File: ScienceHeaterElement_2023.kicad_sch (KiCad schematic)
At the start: 1 part, among them U1 LMT85DCK

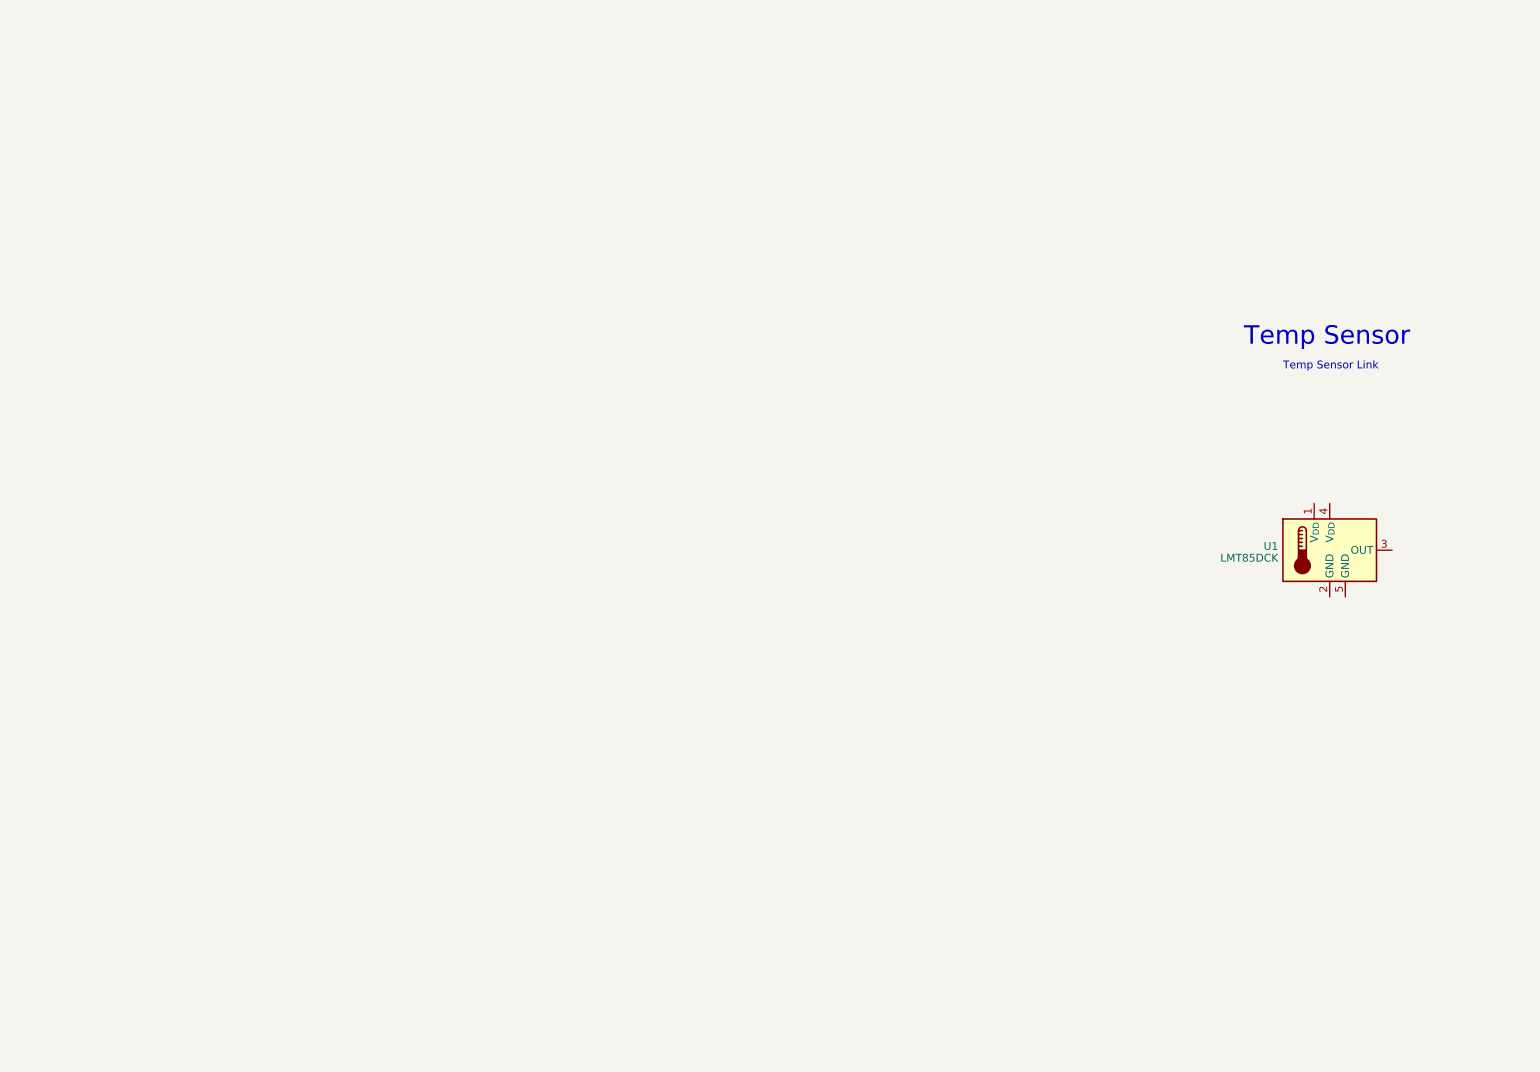
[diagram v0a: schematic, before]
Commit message: Science Heater KiCad
Inserted Anderson components, a temperature sensor and a molex SL.
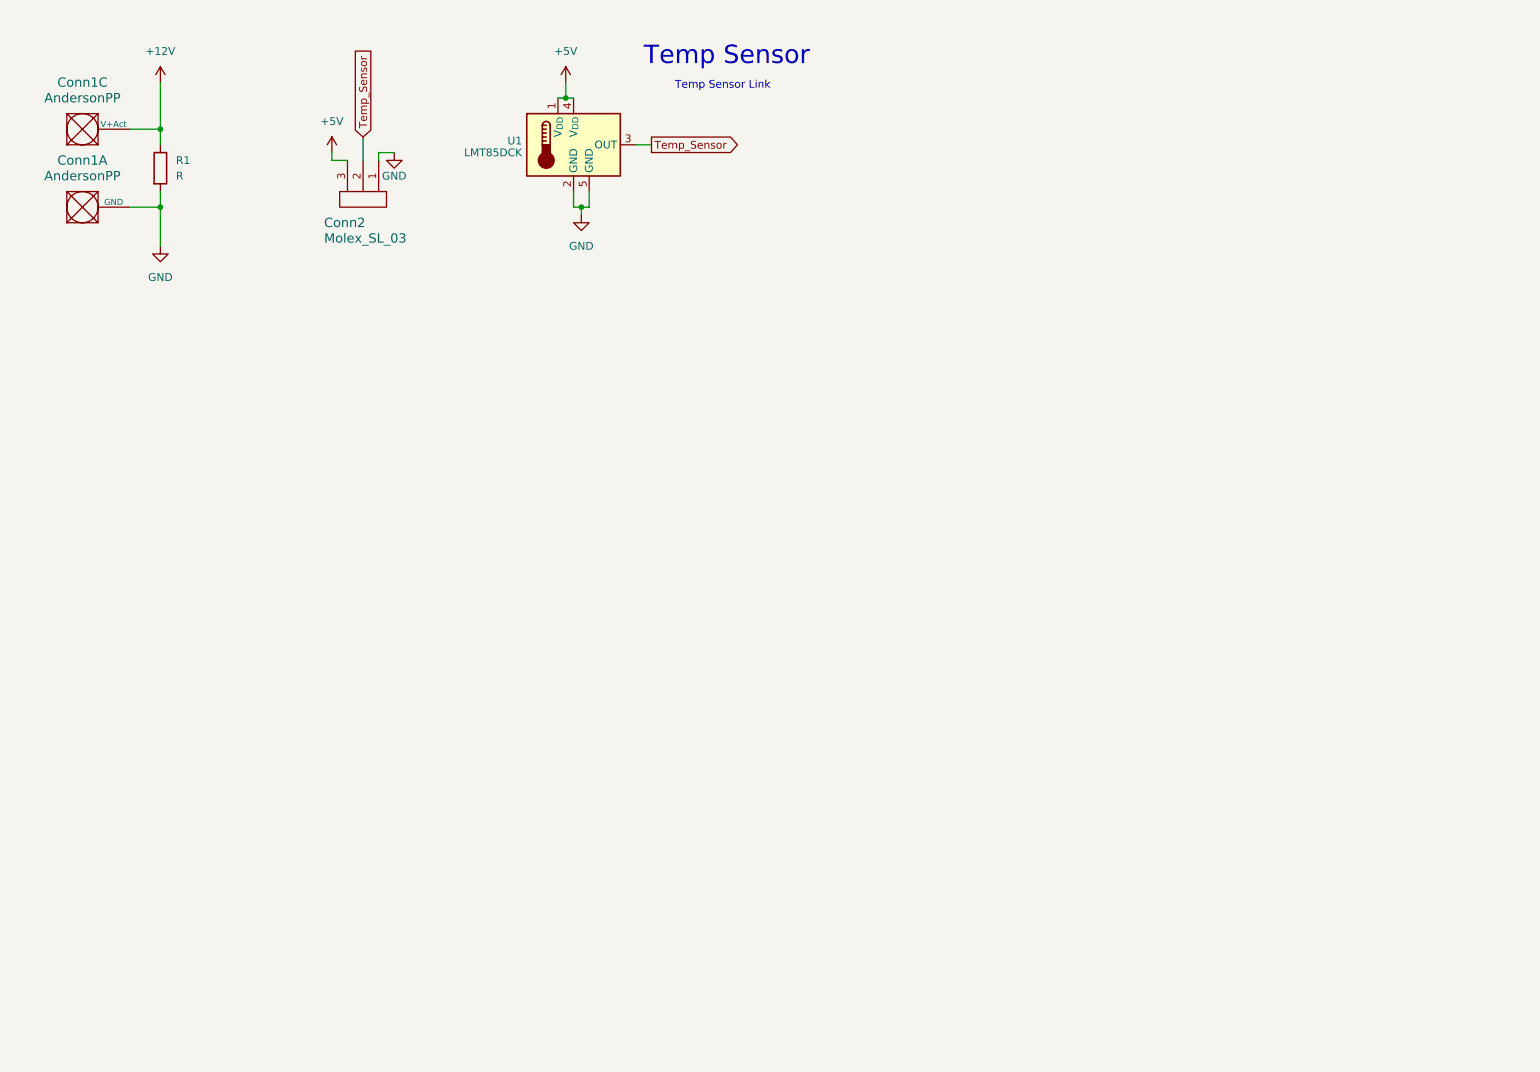
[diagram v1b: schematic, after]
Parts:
- added Conn1: AndersonPP, symbol MRDT_Connectors:AndersonPP
- added Conn2: Molex_SL_03, symbol MRDT_Connectors:Molex_SL_03
- added R1: R, symbol Device:R
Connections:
- net +5V: now reaches U1.1 (V_{DD})
- net +5V: now also U1.4 (V_{DD}), Conn2.3
- net GND: now reaches U1.2 (GND)
- net GND: now also U1.5 (GND), Conn1.1 (GND), Conn2.1, R1.2
- net Temp_Sensor: now reaches U1.3 (OUT)
- net Temp_Sensor: now also Conn2.2
- new net +12V: Conn1.3 (V+Act), R1.1
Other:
- moved on the sheet: U1

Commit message: Added BJT Circuit
Created BJT emitter bias circuit
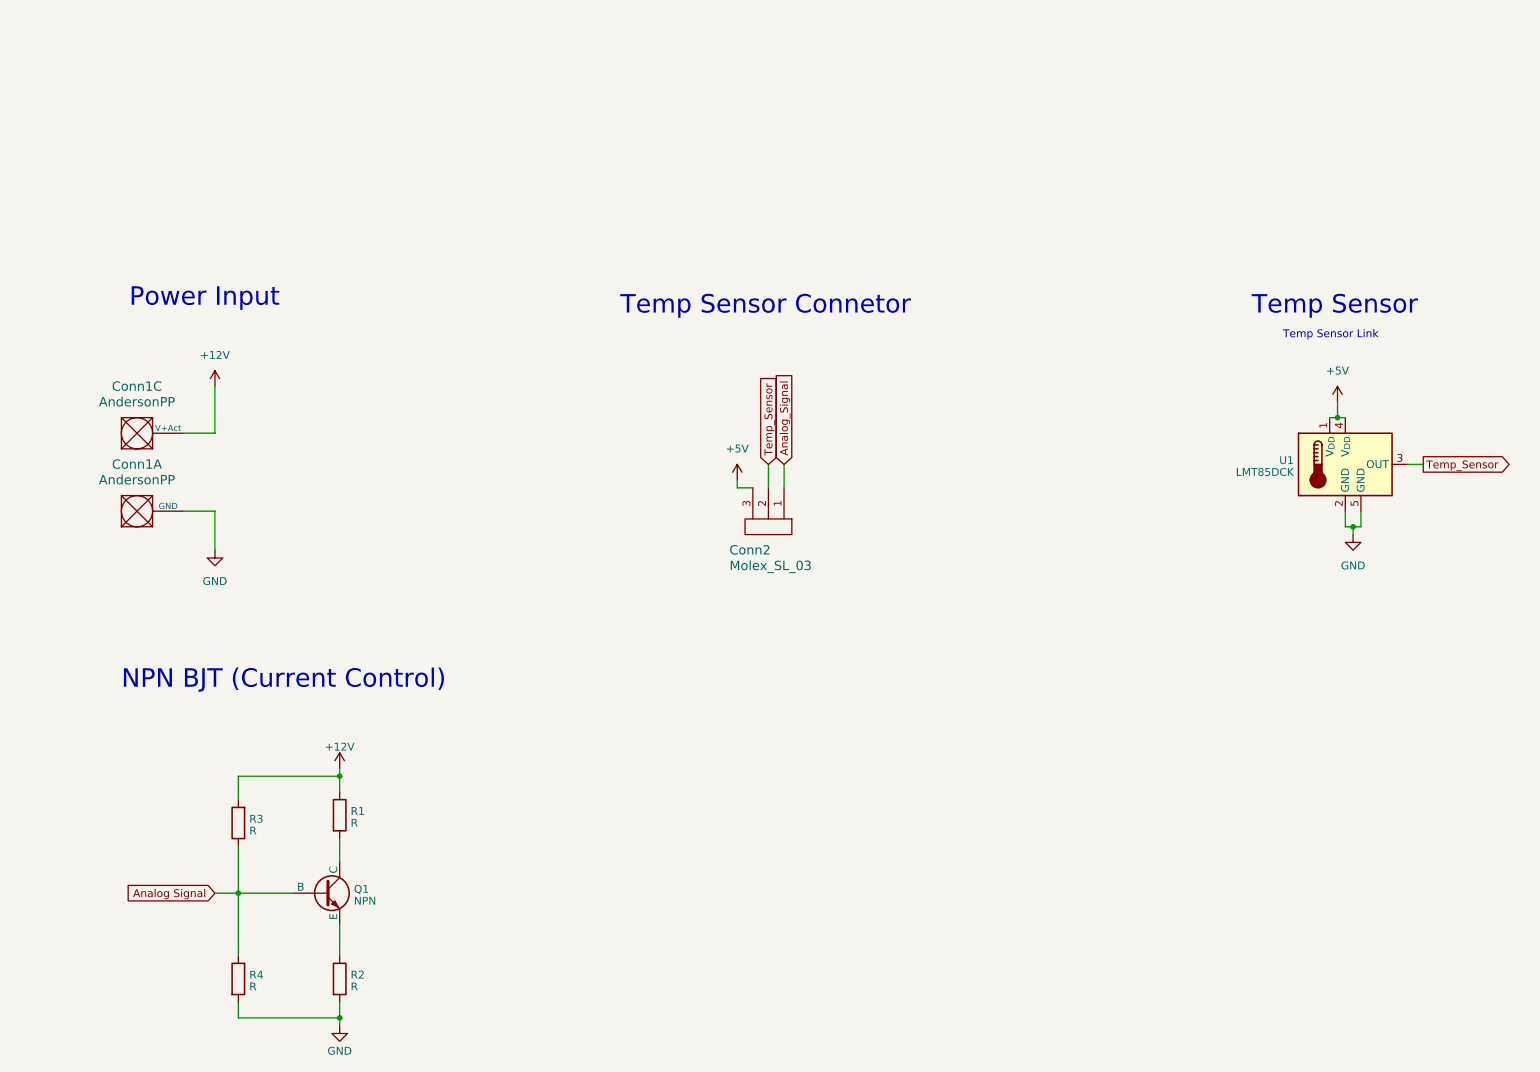
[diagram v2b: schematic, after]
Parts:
- added Q1: NPN, symbol Simulation_SPICE:NPN
- added R2, R3, R4: R, symbol Device:R
- Conn1: footprint (none) -> MRDT_Connectors:MOLEX_SL_02_Horizontal
- Conn2: footprint (none) -> MRDT_Connectors:MOLEX_SL_03_Horizontal
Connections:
- net +12V: now also R3.2
- net GND: now also R2.2, R4.2; no longer Conn2.1, R1.2
- new net: Q1.3 (E), R2.1
- new net: Q1.1 (C), R1.2
- new net Analog Signal: Q1.2 (B), R3.1, R4.1
- new net Analog_Signal: Conn2.1
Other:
- note added: "NPN BJT (Current Control)"
- note added: "Power Input"
- note added: "Temp Sensor Connetor"
- moved on the sheet: Conn1A, Conn1C, Conn2, U1

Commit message: PDR
Changed BJT circuit
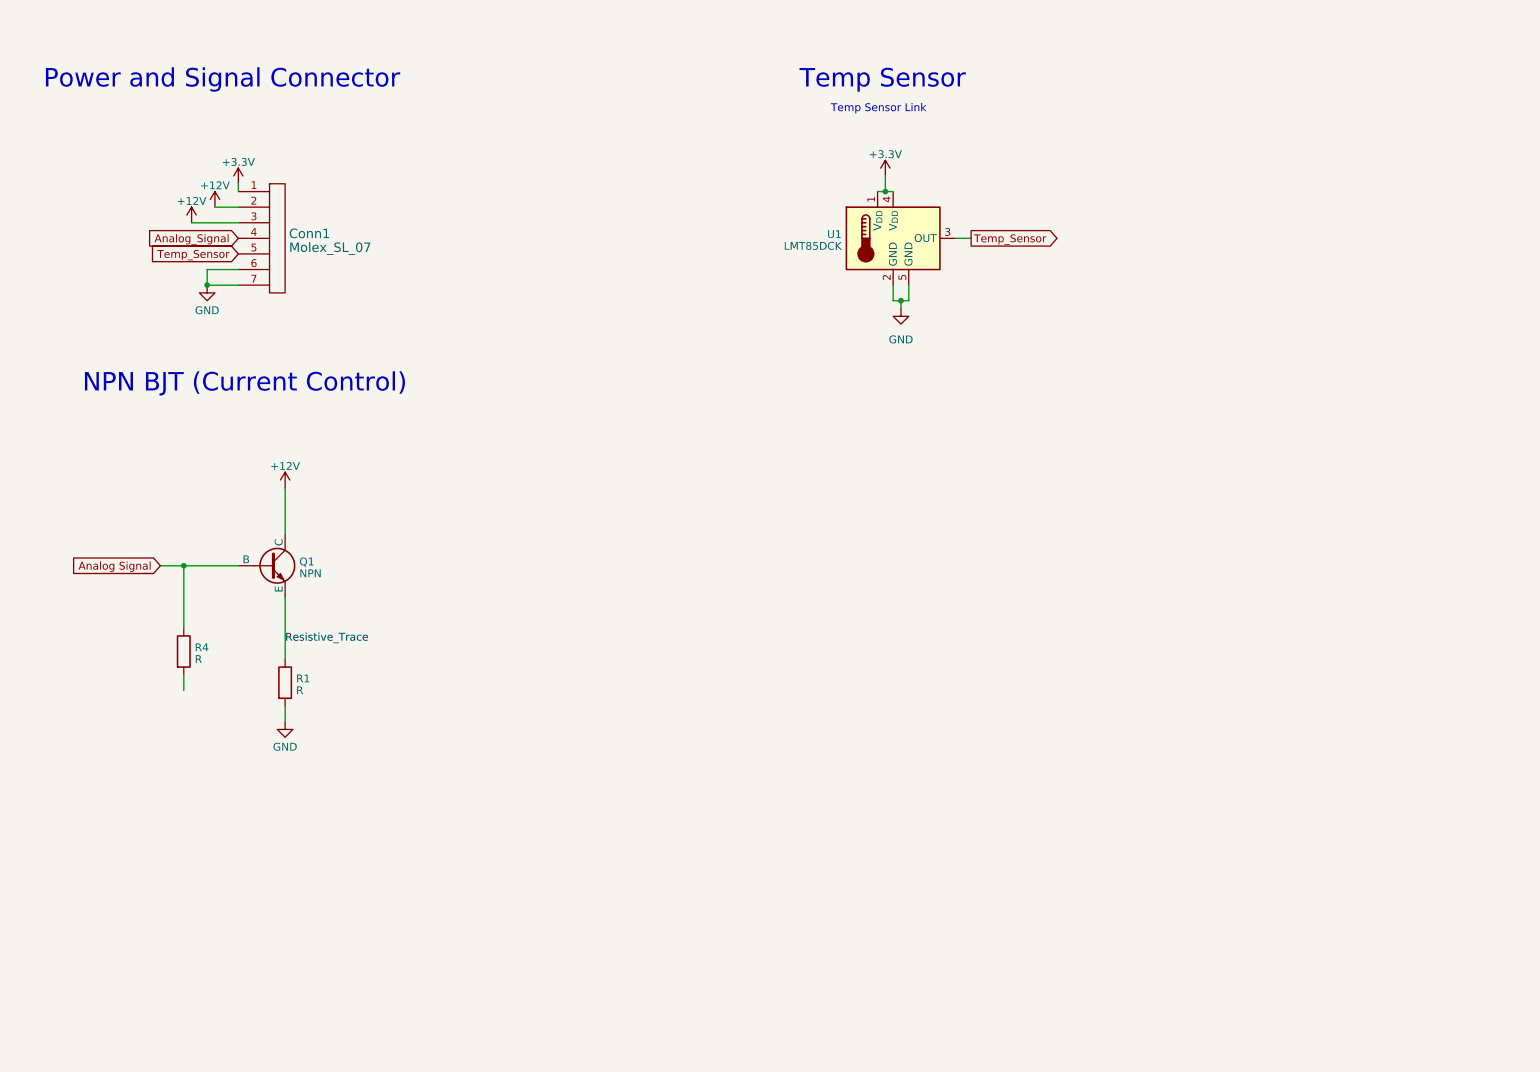
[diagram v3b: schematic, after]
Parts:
- removed Conn1: AndersonPP, MRDT_Connectors:MOLEX_SL_02_Horizontal, symbol MRDT_Connectors:AndersonPP
- removed Conn2: Molex_SL_03, MRDT_Connectors:MOLEX_SL_03_Horizontal, symbol MRDT_Connectors:Molex_SL_03
- removed R2, R3: R, symbol Device:R
- added Conn1: Molex_SL_07, symbol MRDT_Connectors:Molex_SL_07
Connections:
- net +12V: now also Q1.1 (C), Conn1.2, Conn1.3; no longer R1.1
- net Analog_Signal: now also Conn1.4
- net GND: now also R1.2, Conn1.6, Conn1.7; no longer R4.2
- net Temp_Sensor: now also Conn1.5
- net Resistive_Trace: now reaches Q1.3 (E)
- net Resistive_Trace: now also R1.1
- net +5V renamed +3.3V
- net +3.3V: now also Conn1.1
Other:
- note added: "Power and Signal Connector"
- note removed: "Power Input"
- note removed: "Temp Sensor Connetor"
- moved on the sheet: Q1, R4, U1

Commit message: Added LEDs and Resistor values
Added LEDs and Resistor values
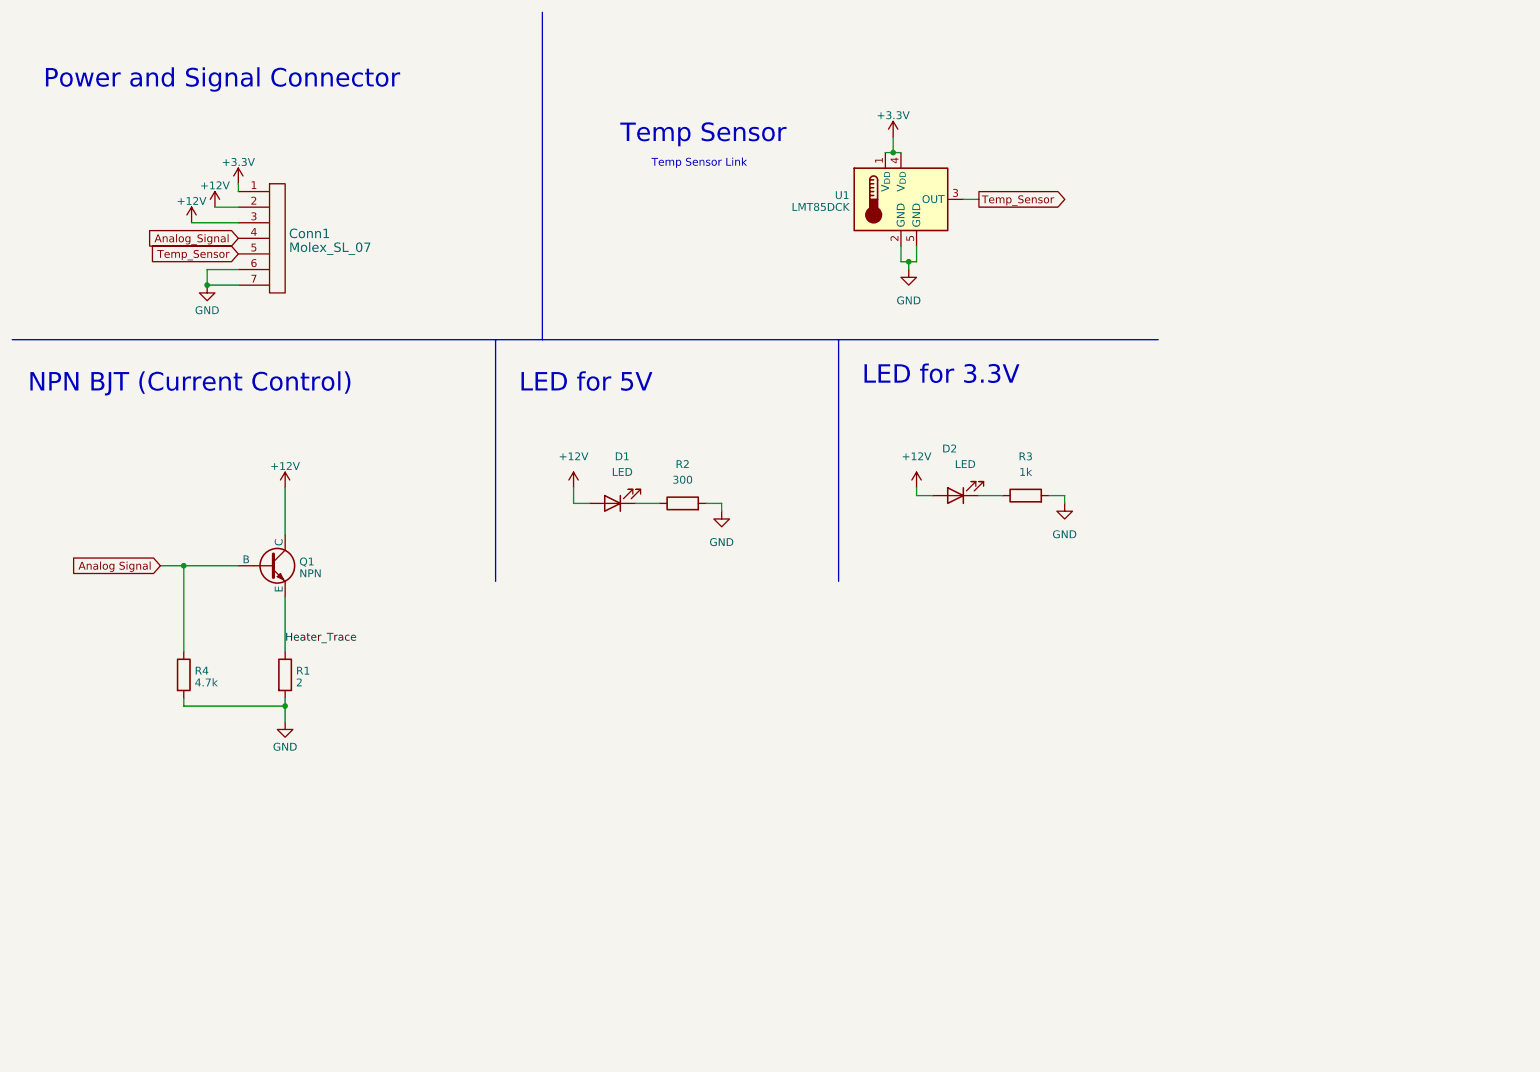
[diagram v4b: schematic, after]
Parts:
- added D1, D2: LED, symbol Device:LED
- added R2: 300, symbol Device:R
- added R3: 1k, symbol Device:R
- R1: value R -> 2
- R4: value R -> 4.7k
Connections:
- net +12V: now also D1.2 (A), D2.2 (A)
- net GND: now also R4.2, R2.2, R3.2
- net Resistive_Trace renamed Heater_Trace
- new net: D1.1 (K), R2.1
- new net: D2.1 (K), R3.1
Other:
- note added: "LED for 3.3V"
- note added: "LED for 5V"
- moved on the sheet: R1, R4, U1
